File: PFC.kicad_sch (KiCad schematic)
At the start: 22 parts, among them U1 UCC38050

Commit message: Changes:  - Added netclasses  - Better footprint for testpoints  - EMI filter
TODO:
 - Route the rest of the board
 - Different versions of the board to make sure its approved on monday
 - Get shunt footprint
 - Figure out wich connections can be jumpered
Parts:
- TP1, TP2, TP3: footprint TestPoint:TestPoint_Pad_1.0x1.0mm -> TestPoint:TestPoint_THTPad_2.5x2.5mm_Drill1.2mm
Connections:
- net CS_L renamed Current_Sense
- net ZCD_L renamed Zero_Cross
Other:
- moved on the sheet: C3, C6, D1, D2, R10, TP3

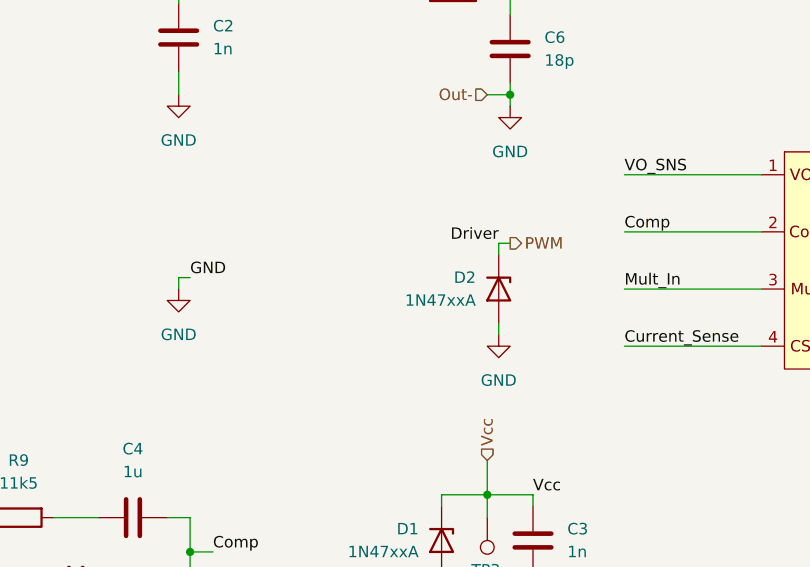
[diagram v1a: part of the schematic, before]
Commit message: Changes:  - Grouped blocks of components for labeling/testing  - Labeled Test conditions on board Todo:  - Arange blocks into a more sensible shape  - Connect them
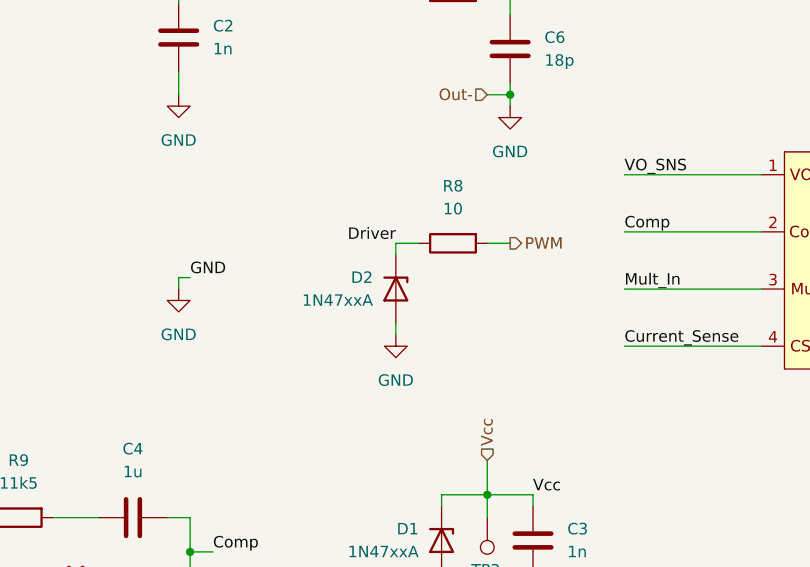
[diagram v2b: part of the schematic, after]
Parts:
- added R8: 10, Resistor_THT:R_Axial_DIN0207_L6.3mm_D2.5mm_P10.16mm_Horizontal, symbol Device:R
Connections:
- net PWM: now also R8.2; no longer D2.1 (K), U1.7
- new net Driver: D2.1 (K), R8.1, U1.7
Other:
- moved on the sheet: D2
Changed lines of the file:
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@@
+	(wire
+		(pts
+			(xy 152.4 90.17) (xy 149.86 90.17)
+		)
+		(stroke
+			(width 0)
+			(type default)
+		)
+	)
 	(wire
 		(pts
@@
 	(wire
 		(pts
-			(xy 161.29 90.17) (xy 161.29 91.44)
+			(xy 149.86 90.17) (xy 149.86 91.44)
 		)
 		(stroke
@@
 	(wire
 		(pts
-			(xy 161.29 99.06) (xy 161.29 100.33)
+			(xy 149.86 99.06) (xy 149.86 100.33)
 		)
 		(stroke
@@
 	(wire
 		(pts
-			(xy 162.56 90.17) (xy 161.29 90.17)
+			(xy 162.56 90.17) (xy 160.02 90.17)
 		)
 		(stroke
@@
 	)
 	(label "Driver"
-		(at 161.29 90.17 180)
+		(at 149.86 90.17 180)
 		(effects
 			(font
@@
 	(symbol
 		(lib_id "Diode:1N47xxA")
-		(at 161.29 95.25 270)
+		(at 149.86 95.25 270)
 		(unit 1)
 		(exclude_from_sim no)
@@
 		(dnp no)
 		(property "Reference" "D2"
-			(at 158.75 93.9799 90)
+			(at 147.32 93.9799 90)
 			(effects
 				(font
@@
 		)
 		(property "Value" "1N47xxA"
-			(at 158.75 96.5199 90)
+			(at 147.32 96.5199 90)
 			(effects
 				(font
@@
 		)
 		(property "Footprint" "Diode_THT:D_DO-41_SOD81_P10.16mm_Horizontal"
-			(at 156.845 95.25 0)
+			(at 145.415 95.25 0)
 			(effects
 				(font
@@
 		)
 		(property "Datasheet" "https://www.vishay.com/docs/85816/1n4728a.pdf"
-			(at 161.29 95.25 0)
+			(at 149.86 95.25 0)
 			(effects
 				(font
@@
 		)
 		(property "Description" "1300mW Silicon planar power Zener diodes, DO-41"
-			(at 161.29 95.25 0)
+			(at 149.86 95.25 0)
 			(effects
 				(font
@@
 	)
 	(symbol
+		(lib_id "Device:R")
+		(at 156.21 90.17 90)
+		(mirror x)
+		(unit 1)
+		(exclude_from_sim no)
+		(in_bom yes)
+		(on_board yes)
+		(dnp no)
+		(fields_autoplaced yes)
+		(property "Reference" "R8"
+			(at 156.21 83.82 90)
+			(effects
+				(font
+					(size 1.27 1.27)
+				)
+			)
+		)
+		(property "Value" "10"
+			(at 156.21 86.36 90)
+			(effects
+				(font
+					(size 1.27 1.27)
+				)
+			)
+		)
+		(property "Footprint" "Resistor_THT:R_Axial_DIN0207_L6.3mm_D2.5mm_P10.16mm_Horizontal"
+			(at 156.21 88.392 90)
+			(effects
+				(font
+					(size 1.27 1.27)
+				)
+				(hide yes)
+			)
+		)
+		(property "Datasheet" "~"
+			(at 156.21 90.17 0)
+			(effects
+				(font
+					(size 1.27 1.27)
+				)
+				(hide yes)
+			)
+		)
+		(property "Description" "Resistor"
+			(at 156.21 90.17 0)
+			(effects
+				(font
+					(size 1.27 1.27)
+				)
+				(hide yes)
+			)
+		)
+		(pin "1"
+		)
+		(pin "2"
+		)
+		(instances
+			(project "ELP2-Boost_PFSC"
+				(path "/75286de1-7f8d-40aa-9455-9b7cb1219971/632fa9e6-e980-4ea8-a4d3-2ac1d8c15c2c"
+					(reference "R8")
+					(unit 1)
+				)
+			)
+		)
+	)
+	(symbol
 		(lib_id "Connector:TestPoint")
 		(at 160.02 120.65 0)
@@
 	(symbol
 		(lib_id "power:GND")
-		(at 161.29 100.33 0)
+		(at 149.86 100.33 0)
 		(unit 1)
 		(exclude_from_sim no)
@@
 		(fields_autoplaced yes)
 		(property "Reference" "#PWR06"
-			(at 161.29 106.68 0)
+			(at 149.86 106.68 0)
 			(effects
 				(font
@@
 		)
 		(property "Value" "GND"
-			(at 161.29 105.41 0)
+			(at 149.86 105.41 0)
 			(effects
 				(font
@@
 		)
 		(property "Footprint" ""
-			(at 161.29 100.33 0)
+			(at 149.86 100.33 0)
 			(effects
 				(font
@@
 		)
 		(property "Datasheet" ""
-			(at 161.29 100.33 0)
+			(at 149.86 100.33 0)
 			(effects
 				(font
@@
 		)
 		(property "Description" "Power symbol creates a global label with name \"GND\" , ground"
-			(at 161.29 100.33 0)
-			(effects
-				(font
+			(at 149.86 100.33 0)
+			(effects
+				(font

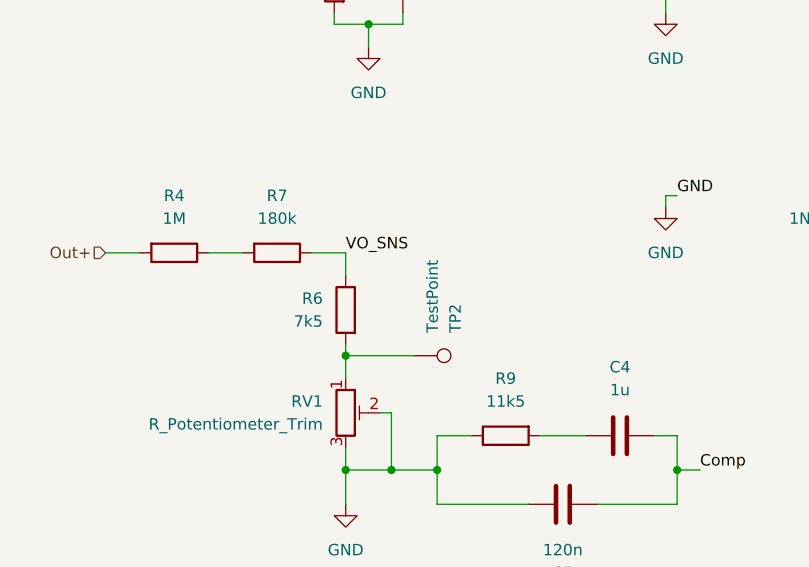
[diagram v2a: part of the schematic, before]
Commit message: Changes:  - Added ground plane for analog components  - Better EMI shielding on UCC and MOSFET TODO:  - Try and get everything closer, somehow
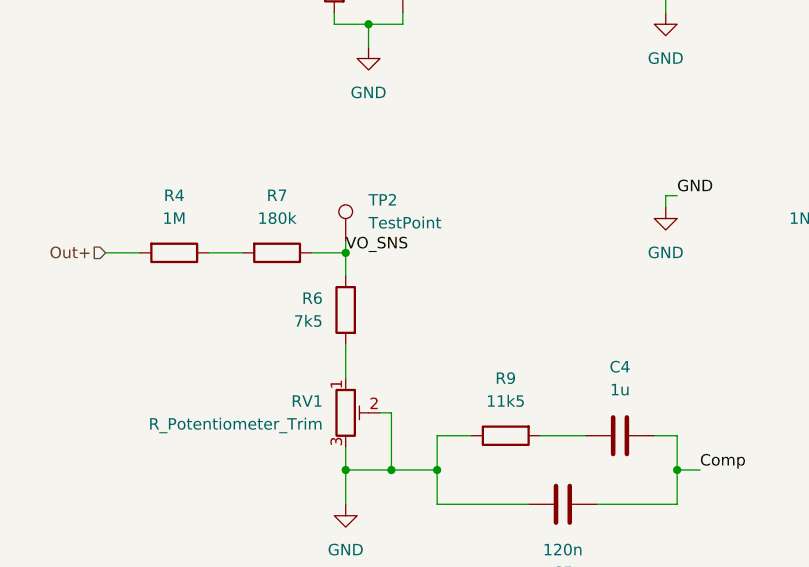
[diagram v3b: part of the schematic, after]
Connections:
- net VO_SNS: now also TP2.1
- net at R6.2, RV1.1: no longer TP2.1
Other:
- moved on the sheet: TP2
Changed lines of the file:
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@@
+	)
+	(junction
+		(at 90.17 100.33)
+		(diameter 0)
+		(color 0 0 0 0)
 	)
 	(junction
@@
 	)
 	(junction
-		(at 90.17 111.76)
-		(diameter 0)
-		(color 0 0 0 0)
-	)
-	(junction
 		(at 160.02 118.11)
 		(diameter 0)
@@
 	(wire
 		(pts
+			(xy 90.17 99.06) (xy 90.17 100.33)
+		)
+		(stroke
+			(width 0)
+			(type default)
+		)
+	)
+	(wire
+		(pts
 			(xy 160.02 128.27) (xy 165.1 128.27)
 		)
@@
 	(wire
 		(pts
-			(xy 97.79 111.76) (xy 90.17 111.76)
-		)
-		(stroke
-			(width 0)
-			(type default)
-		)
-	)
-	(wire
-		(pts
 			(xy 121.92 60.96) (xy 125.73 60.96)
 		)
@@
 	(wire
 		(pts
-			(xy 90.17 111.76) (xy 90.17 114.3)
+			(xy 90.17 110.49) (xy 90.17 114.3)
 		)
 		(stroke
@@
 		(pts
 			(xy 92.71 60.96) (xy 92.71 63.5)
-		)
-		(stroke
-			(width 0)
-			(type default)
-		)
-	)
-	(wire
-		(pts
-			(xy 90.17 110.49) (xy 90.17 111.76)
 		)
 		(stroke
@@
 	(symbol
 		(lib_id "Connector:TestPoint")
-		(at 97.79 111.76 270)
-		(mirror x)
+		(at 90.17 99.06 0)
 		(unit 1)
 		(exclude_from_sim no)
@@
 		(dnp no)
 		(property "Reference" "TP2"
-			(at 102.3621 109.22 0)
+			(at 92.71 94.4879 0)
 			(effects
 				(font
@@
 		)
 		(property "Value" "TestPoint"
-			(at 99.8221 109.22 0)
+			(at 92.71 97.0279 0)
 			(effects
 				(font
@@
 		)
 		(property "Footprint" "TestPoint:TestPoint_THTPad_2.5x2.5mm_Drill1.2mm"
-			(at 97.79 106.68 0)
+			(at 95.25 99.06 0)
 			(effects
 				(font
@@
 		)
 		(property "Datasheet" "~"
-			(at 97.79 106.68 0)
+			(at 95.25 99.06 0)
 			(effects
 				(font
@@
 		)
 		(property "Description" "test point"
-			(at 97.79 111.76 0)
-			(effects
-				(font
+			(at 90.17 99.06 0)
+			(effects
+				(font

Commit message: Placa refeita de acordo com pedidos do professor, sujeita a alteração
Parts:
- removed RV1: R_Potentiometer_Trim, ELP-Boost_PFC:Trimpot-10k, symbol Device:R_Potentiometer_Trim
- C1, C2, C3, C6: footprint Capacitor_THT:C_Disc_D5.0mm_W2.5mm_P2.50mm -> Capacitor_THT:C_Disc_D5.0mm_W2.5mm_P5.00mm
- C4: footprint Capacitor_THT:C_Rect_L9.0mm_W2.5mm_P7.50mm_MKT -> Capacitor_THT:C_Disc_D5.0mm_W2.5mm_P5.00mm
- C5: footprint Capacitor_THT:C_Rect_L13.5mm_W5.0mm_P10.00mm_FKS3_FKP3_MKS4 -> Capacitor_THT:C_Disc_D5.0mm_W2.5mm_P5.00mm
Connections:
- net GND: now also R6.2
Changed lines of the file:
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@@
 	(paper "A4")
-	(junction
-		(at 95.25 124.46)
-		(diameter 0)
-		(color 0 0 0 0)
-	)
 	(junction
 		(at 92.71 63.5)
@@
 	(wire
 		(pts
-			(xy 93.98 118.11) (xy 95.25 118.11)
-		)
-		(stroke
-			(width 0)
-			(type default)
-		)
-	)
-	(wire
-		(pts
 			(xy 74.93 100.33) (xy 78.74 100.33)
 		)
@@
 	(wire
 		(pts
+			(xy 90.17 110.49) (xy 90.17 124.46)
+		)
+		(stroke
+			(width 0)
+			(type default)
+		)
+	)
+	(wire
+		(pts
 			(xy 125.73 63.5) (xy 125.73 60.96)
 		)
@@
 	(wire
 		(pts
-			(xy 90.17 121.92) (xy 90.17 124.46)
-		)
-		(stroke
-			(width 0)
-			(type default)
-		)
-	)
-	(wire
-		(pts
 			(xy 127 120.65) (xy 124.46 120.65)
 		)
@@
 	(wire
 		(pts
+			(xy 90.17 100.33) (xy 93.98 100.33)
+		)
+		(stroke
+			(width 0)
+			(type default)
+		)
+	)
+	(wire
+		(pts
 			(xy 121.92 60.96) (xy 125.73 60.96)
 		)
@@
 	(wire
 		(pts
-			(xy 90.17 124.46) (xy 95.25 124.46)
-		)
-		(stroke
-			(width 0)
-			(type default)
-		)
-	)
-	(wire
-		(pts
-			(xy 95.25 124.46) (xy 100.33 124.46)
+			(xy 90.17 124.46) (xy 100.33 124.46)
 		)
 		(stroke
@@
 	(wire
 		(pts
-			(xy 90.17 110.49) (xy 90.17 114.3)
-		)
-		(stroke
-			(width 0)
-			(type default)
-		)
-	)
-	(wire
-		(pts
 			(xy 154.94 127) (xy 154.94 128.27)
 		)
@@
 		(pts
 			(xy 154.94 118.11) (xy 154.94 119.38)
-		)
-		(stroke
-			(width 0)
-			(type default)
-		)
-	)
-	(wire
-		(pts
-			(xy 95.25 118.11) (xy 95.25 124.46)
 		)
 		(stroke
@@
 		)
 	)
-	(label "VO_SNS"
-		(at 90.17 100.33 0)
-		(effects
-			(font
-				(size 1.27 1.27)
-			)
-			(justify left bottom)
-		)
-	)
 	(label "Driver"
 		(at 149.86 90.17 180)
@@
 	(label "Zero_Cross"
 		(at 162.56 62.23 0)
+		(effects
+			(font
+				(size 1.27 1.27)
+			)
+			(justify left bottom)
+		)
+	)
+	(label "VO_SNS"
+		(at 93.98 100.33 0)
 		(effects
 			(font
@@
 			)
 		)
-		(property "Footprint" "Capacitor_THT:C_Disc_D5.0mm_W2.5mm_P2.50mm"
+		(property "Footprint" "Capacitor_THT:C_Disc_D5.0mm_W2.5mm_P5.00mm"
 			(at 166.0652 127 0)
 			(effects
@@
 			)
 		)
-		(property "Footprint" "Capacitor_THT:C_Rect_L9.0mm_W2.5mm_P7.50mm_MKT"
+		(property "Footprint" "Capacitor_THT:C_Disc_D5.0mm_W2.5mm_P5.00mm"
 			(at 116.84 119.6848 0)
 			(effects
@@
 	)
 	(symbol
-		(lib_id "Device:R_Potentiometer_Trim")
-		(at 90.17 118.11 0)
-		(unit 1)
-		(exclude_from_sim no)
-		(in_bom yes)
-		(on_board yes)
-		(dnp no)
-		(fields_autoplaced yes)
-		(property "Reference" "RV1"
-			(at 87.63 116.8399 0)
-			(effects
-				(font
-					(size 1.27 1.27)
-				)
-				(justify right)
-			)
-		)
-		(property "Value" "R_Potentiometer_Trim"
-			(at 87.63 119.3799 0)
-			(effects
-				(font
-					(size 1.27 1.27)
-				)
-				(justify right)
-			)
-		)
-		(property "Footprint" "ELP-Boost_PFC:Trimpot-10k"
-			(at 90.17 118.11 0)
-			(effects
-				(font
-					(size 1.27 1.27)
-				)
-				(hide yes)
-			)
-		)
-		(property "Datasheet" "~"
-			(at 90.17 118.11 0)
-			(effects
-				(font
-					(size 1.27 1.27)
-				)
-				(hide yes)
-			)
-		)
-		(property "Description" "Trim-potentiometer"
-			(at 90.17 118.11 0)
-			(effects
-				(font
-					(size 1.27 1.27)
-				)
-				(hide yes)
-			)
-		)
-		(pin "1"
-		)
-		(pin "3"
-		)
-		(pin "2"
-		)
-		(instances
-			(project ""
-				(path "/75286de1-7f8d-40aa-9455-9b7cb1219971/632fa9e6-e980-4ea8-a4d3-2ac1d8c15c2c"
-					(reference "RV1")
-					(unit 1)
-				)
-			)
-		)
-	)
-	(symbol
 		(lib_id "Device:C")
 		(at 96.52 69.85 0)
@@
 			)
 		)
-		(property "Footprint" "Capacitor_THT:C_Disc_D5.0mm_W2.5mm_P2.50mm"
+		(property "Footprint" "Capacitor_THT:C_Disc_D5.0mm_W2.5mm_P5.00mm"
 			(at 97.4852 73.66 0)
 			(effects
@@
 		)
 		(property "Value" "TestPoint"
-			(at 92.71 97.0279 0)
+			(at 87.63 92.71 0)
 			(effects
 				(font
@@
 			)
 		)
-		(property "Footprint" "Capacitor_THT:C_Disc_D5.0mm_W2.5mm_P2.50mm"
+		(property "Footprint" "Capacitor_THT:C_Disc_D5.0mm_W2.5mm_P5.00mm"
 			(at 126.6952 71.12 0)
 			(effects
@@
 			)
 		)
-		(property "Footprint" "Capacitor_THT:C_Disc_D5.0mm_W2.5mm_P2.50mm"
+		(property "Footprint" "Capacitor_THT:C_Disc_D5.0mm_W2.5mm_P5.00mm"
 			(at 163.5252 72.39 0)
 			(effects
@@
 			)
 		)
-		(property "Footprint" "Capacitor_THT:C_Rect_L13.5mm_W5.0mm_P10.00mm_FKS3_FKP3_MKS4"
+		(property "Footprint" "Capacitor_THT:C_Disc_D5.0mm_W2.5mm_P5.00mm"
 			(at 110.49 129.2352 0)
 			(effects
